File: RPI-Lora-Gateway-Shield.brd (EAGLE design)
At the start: 99.1 x 99.1 mm, 62 parts, among them J1 GROVE, J10 CON_TERMINAL_BLOCK_02-5MM, J11 JUMPER_1X30805, J12 JUMPER_1X30805, J13 GROVE I2C, J14 2.54_I2C, J15 POWER_JACKPTH, J16 2.54_PWR, J4 RASPBERRYPI-40-PIN-GPIO, J5 DHTxx, J6 2.54_I2C, J7 2.54_I2C, J8 CON_TERMINAL_BLOCK_02-5MM, J9 CON_TERMINAL_BLOCK_02-5MM

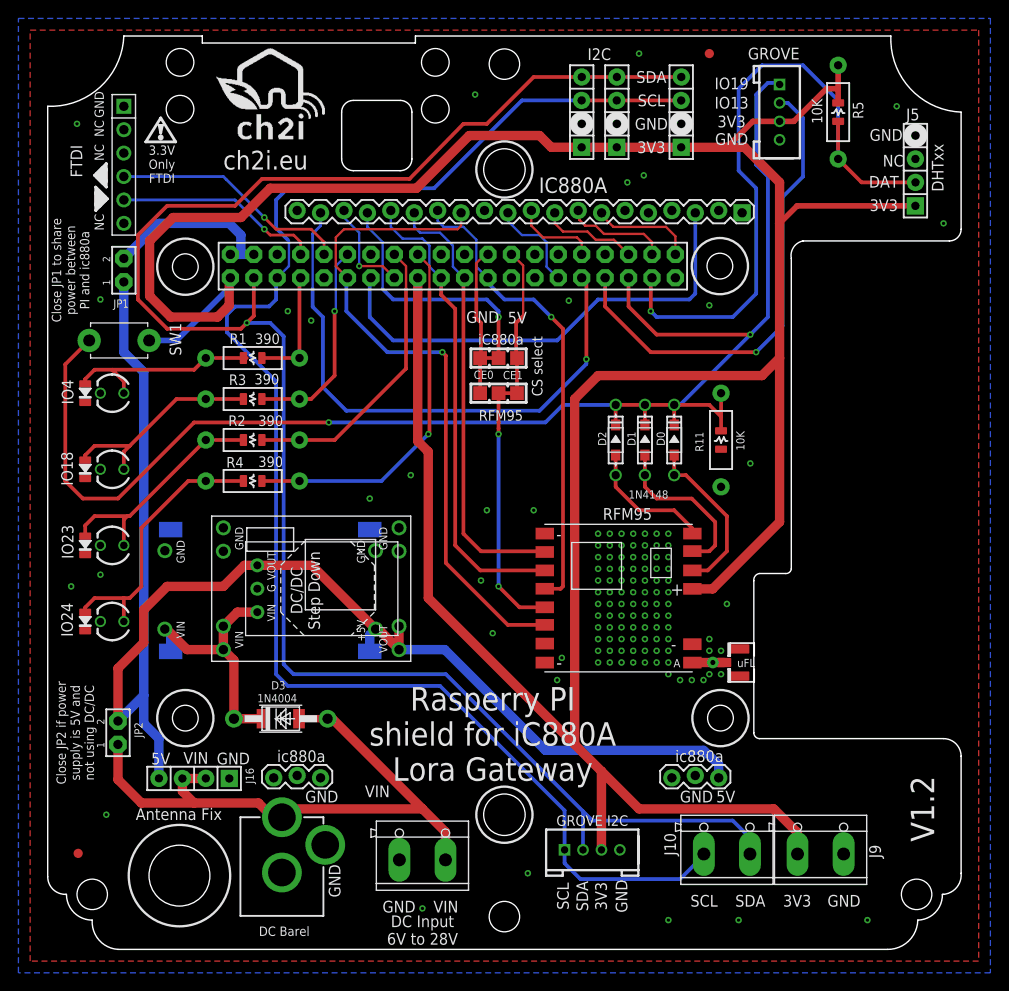
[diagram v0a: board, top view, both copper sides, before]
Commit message: removed RFM9x, added GPS Module + INA219 current sensor
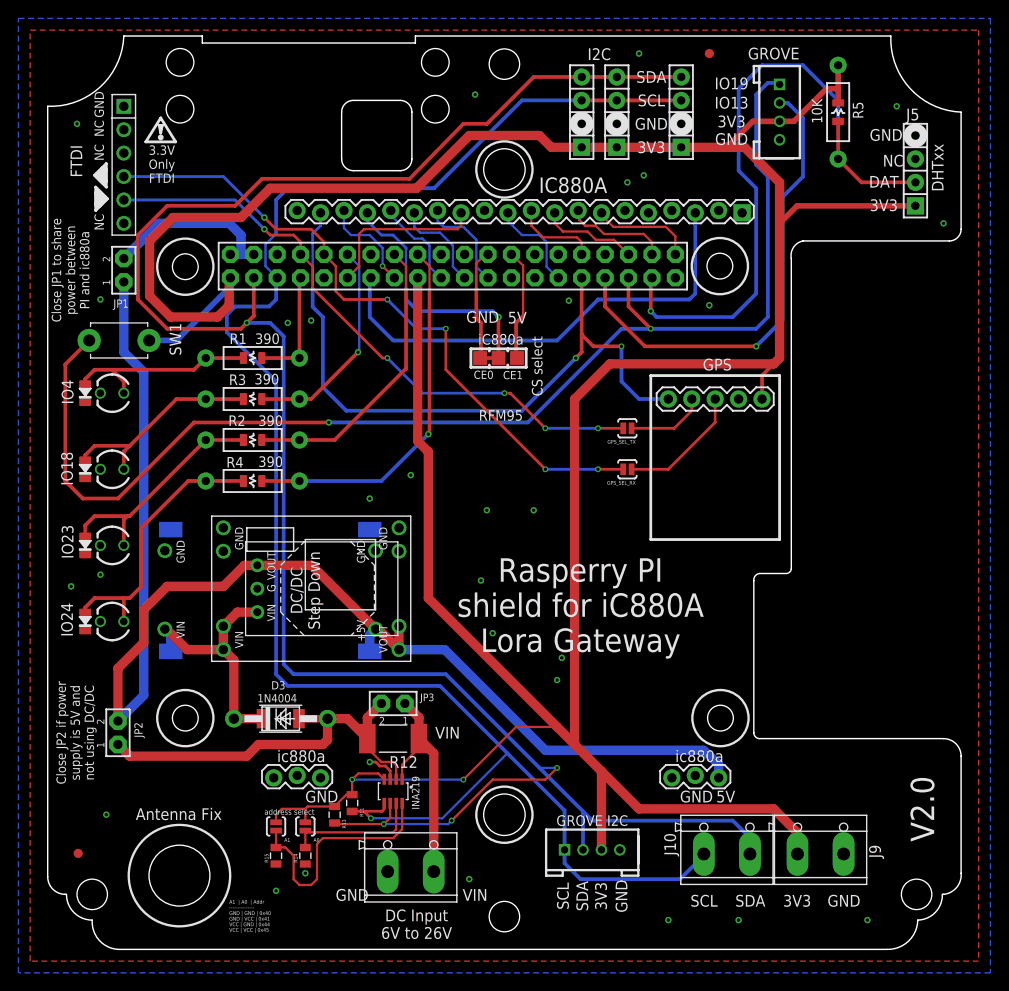
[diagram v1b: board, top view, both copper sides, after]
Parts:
- removed D0, D1, D2: 1N4148, Seeed-Discrete:SOD123-2.7X1.6
- removed D5: 1N4148, adafruit:DO-1N4148
- removed D6, D7: (no value), adafruit:DO-1N4148
- removed J12: JUMPER_1X30805, dp_devices:JP3_0805
- removed J15: POWER_JACKPTH, SparkFun-Connectors:POWER_JACK_PTH
- removed J16: 2.54_PWR, _c2h:1X04_NO_LOCK
- removed U$1, U$9: (no value), _c2h:LOGO_CH2I_110MM
- removed U$2: RFM95, _c2h:RFM95
- removed U$3: ANTENNA-UFL, _c2h:UFL_PAD
- added A0, A1, GPS_SEL_RX, GPS_SEL_TX: SOLDERJUMPERNO, SparkFun-Retired:SJ_2S-NO
- added GPS: (no value), SparkFun-Connectors:1X05
- added INA219: (no value), INA219:SOT23-8
- added JP3: (no value), microbuilder:JUMPER2
- added R13, R14, R15: 10K, SparkFun-Passives:0805
- R11: device _c2h:AXIAL-0.4 -> SparkFun-Passives:0805
- R12: device _c2h:0805-RES -> adafruit:R2512
- moved R11 56.1 mm to (33.0, 15.9), turned to 270 degrees
- moved R12 48.1 mm to (37.5, 22.9), turned to 180 degrees
- moved J8 1.80 mm to (39.4, 8.89)
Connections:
- removed net DIO0: D0.1, D6.A, U$2.DIO0
- removed net DIO1: D1.1, D7.A, U$2.DIO1
- removed net DIO2: D2.1, D5.A, U$2.DIO2
- removed net N$29: U$2.ANT, U$3.ANT1, U$3.ANT2
- removed net SPI_SEL: J12.2, U$2.NSS
- new net A0: A0.1, INA219.7, R14.2
- new net A1: A1.1, INA219.8, R15.2
- new net RX: GPS.2, GPS_SEL_TX.1
- new net TX: GPS.3, GPS_SEL_RX.1
- new net VIN+: INA219.1, J8.1, JP3.1, R12.1
- net +5V: no longer J16.4
- net 3V3: now also A0.2, A1.2, GPS.5, INA219.4, R11.1, R13.1; no longer U$2.VDD
- net GND: now also GPS.4, INA219.3, R14.1, R15.1; no longer J15.GND, J15.GNDBREAK, J16.1, R11.P$1, R12.1, U$2.GND, U$2.GND1, U$2.GND2, U$3.GND1, U$3.GND2
- net GPIO19: no longer D0.2, D1.2, D2.2, D5.C, D6.C, D7.C, R11.P$2, R12.2
- net GPS_PPS: now also GPS.1
- net RXI: now also GPS_SEL_RX.2
- net SCL: now also INA219.5, R11.2
- net SDA: now also INA219.6, R13.2
- net SPI_CE0: no longer J12.1
- net SPI_CE1: no longer J12.3
- net SPI_MISO: no longer U$2.MISO
- net SPI_MOSI: no longer U$2.MOSI
- net SPI_SCLK: no longer U$2.SCK
- net SX_RST: no longer U$2.RST
- net TXO: now also GPS_SEL_TX.2
- net VIN: now also INA219.2, JP3.2, R12.2; no longer J15.PWR, J16.2, J16.3, J8.1
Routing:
- net SX_RST: track 72.9 -> 18.1 mm, vias 1 -> 0
- net RXI: track 26.0 -> 72.3 mm, vias 1 -> 5
- net TXO: track 22.4 -> 66.6 mm, vias 1 -> 5
- net SPI_MOSI: track 51.4 -> 10.1 mm
- net SPI_SCLK: track 51.6 -> 10.9 mm, vias 1 -> 0
- net SPI_MISO: track 48.1 -> 10.6 mm
- net SDA: track 196.1 -> 227.3 mm, vias 1 -> 4
- net GPIO19: track 163.2 -> 135.8 mm
- net SPI_SEL: track 26.9 -> 0.00 mm, vias 2 -> 0
- net A1: track 0.00 -> 26.2 mm
- net VIN+: track 0.00 -> 24.7 mm
- net VIN: track 68.6 -> 45.5 mm
- net SCL: track 167.7 -> 190.6 mm, vias 0 -> 1
- net DIO0: track 18.2 -> 0.00 mm
- net DIO1: track 17.9 -> 0.00 mm
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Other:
- board text added: "A1 | A0 | Addr --------------- GND | GND | 0x40 GND | VCC | 0x41 VCC | GND | 0x44 VCC | VCC | 0x45"
- board text added: "DC Input 6V to 26V"
- board text added: "V2.0"
- board text added: "address select"
- board text removed: "DC Barel"
- board text removed: "DC Input 6V to 28V"
- board text removed: "V1.2"
- board text removed: "ch2i.eu"
- board text removed: "http://ch2i.eu"

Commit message: added header for volt meter + holes for rasppi zero
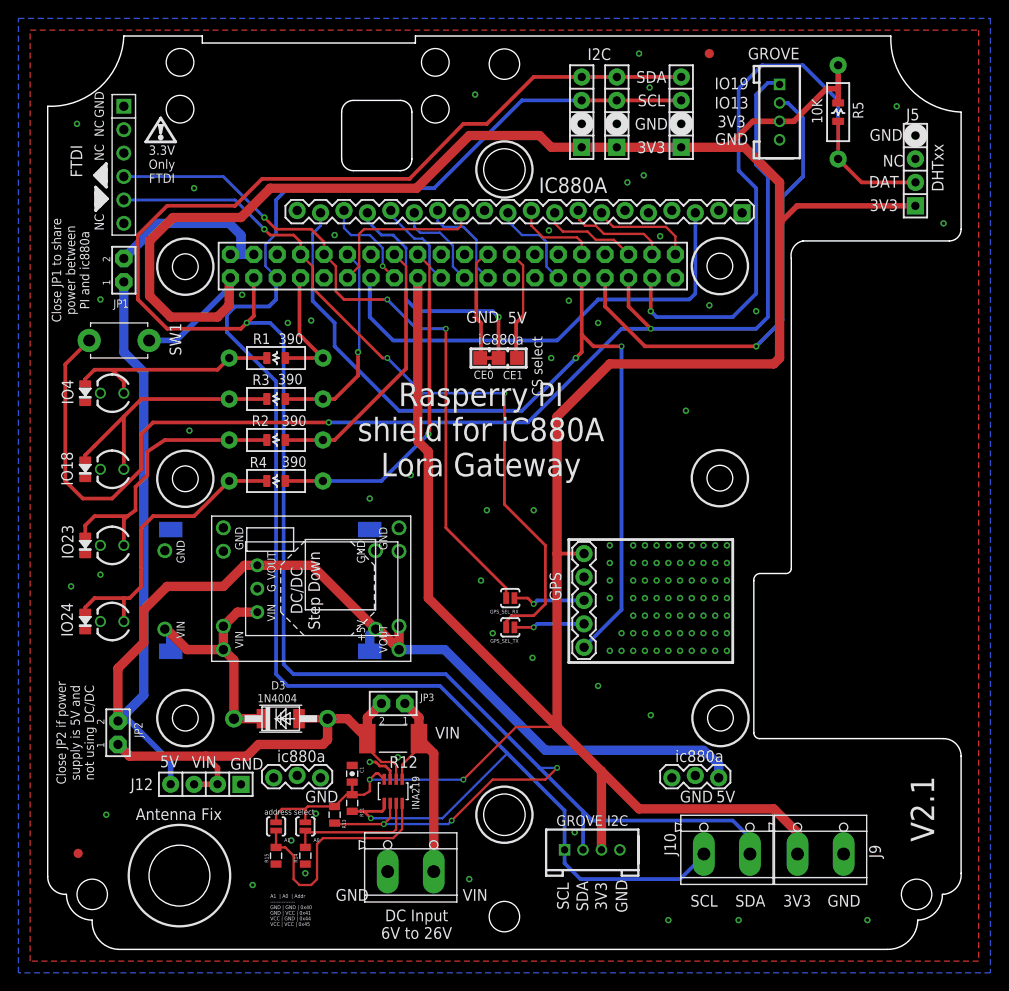
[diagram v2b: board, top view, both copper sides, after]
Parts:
- added C1: 0.1uF, SparkFun-Capacitors:0805-CAP
- added J12: 2.54_PWR, _c2h:1X04_NO_LOCK
- moved GPS 28.4 mm to (58.2, 32.8), turned to 90 degrees
- moved GPS_SEL_TX 25.0 mm to (50.2, 34.9)
- moved GPS_SEL_RX 18.9 mm to (50.2, 38.1)
- moved R1 2.54 mm to (24.8, 64.1)
- moved R2 2.54 mm to (24.8, 55.2)
- moved R3 2.54 mm to (24.8, 59.7)
- moved R4 2.54 mm to (24.8, 50.8)
- moved R6 2.54 mm to (24.8, 64.1)
- moved R7 2.54 mm to (24.8, 55.2)
- moved R8 2.54 mm to (24.8, 59.7)
- moved R9 2.54 mm to (24.8, 50.8)
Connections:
- net +5V: now also J12.4
- net 3V3: now also C1.2
- net GND: now also C1.1, J12.1
- net VIN: now also J12.2, J12.3
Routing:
- net GPS_PPS: track 74.1 -> 95.4 mm
- net TXO: track 66.6 -> 82.5 mm, vias 5 -> 3
- net +5V: track 142.8 -> 152.8 mm
- net VIN: track 45.5 -> 51.6 mm
- net TX: track 13.7 -> 7.97 mm, vias 0 -> 1
- net N$27: track 23.0 -> 28.5 mm
- net N$26: track 25.5 -> 30.8 mm
- net 3V3: track 364.9 -> 360.6 mm
- net RXI: track 72.3 -> 76.1 mm, vias 5 -> 3
- net GPIO24: track 40.2 -> 37.7 mm
- net N$18: track 21.7 -> 24.2 mm
- net N$16: track 29.6 -> 32.2 mm
- net GPIO23: track 31.8 -> 29.2 mm
- net GPIO19: track 135.8 -> 138.0 mm
- net GPIO4: track 12.8 -> 13.9 mm
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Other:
- board text added: "V2.1"
- board text removed: "RFM95"
- board text removed: "V2.0"
